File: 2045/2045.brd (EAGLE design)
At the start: 57.8 x 216.2 mm, 47 parts, among them IC1 OPA2134P, IC2 OPA2134P, X1 2516-

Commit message: upated the 2045 filter
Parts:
- added C13, C14: (no value), dan:E2,5-7
- added D4, D5, D6, D7: 1N4148DO35-7, dan:DO35-7
- added IN1POT, IN2POT: US-EVUF2J, dan:EVUFXJ
- added R25, R51: 10, dan:0207/2V
- C5, C6, C7: device dan:E3,5-10 -> dan:E2,5-7
- R1, R10, R11, R12, R13, R14, R15, R2, R3, R4, R5, R6, R7, R8, R9: device dan:0309/12 -> dan:0204/7
- moved C12 75.7 mm to (48.3, 15.2), turned to 270 degrees
- moved C11 55.5 mm to (22.2, 31.1), turned to 180 degrees
- moved IN2 23.8 mm to (44.5, 139.7)
- moved IN 23.7 mm to (14.0, 139.7)
- moved Q 23.3 mm to (45.1, 204.5)
- moved CVA 23.1 mm to (29.2, 184.8)
- moved R8 20.4 mm to (17.1, 154.3), turned to 0 degrees
- moved R15 18.8 mm to (43.8, 193.7), turned to 0 degrees
- moved CVIN 14.1 mm to (29.2, 139.7)
- moved 2POUT 10.3 mm to (44.5, 122.6)
- moved 4POUTPUT 10.0 mm to (14.0, 122.6)
- moved R7 9.94 mm to (41.3, 154.3), turned to 180 degrees
- moved R14 9.44 mm to (14.6, 191.8), turned to 180 degrees
- moved C6 7.62 mm to (49.5, 66.7)
- moved FC 7.41 mm to (13.3, 204.5)
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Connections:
- new net N$35: IN.P$3, IN1POT.3
- new net N$36: IN2.P$3, IN2POT.3
- new net N$37: D6.C, D7.C, R51.2
- new net N$38: D4.A, D5.A, R25.2
- new net N$71: D7.A, X1.10, X1.9
- new net N$72: D4.C, X1.1, X1.2
- net +12V: now also C13.+, R51.1; no longer X1.10, X1.9
- net -12V: now also C14.-, R25.1; no longer X1.1, X1.2
- net GND: now also C13.-, C14.+, D5.C, D6.A, IN1POT.1, IN2POT.1
- net N$15: now also IN1POT.2; no longer IN.P$3
- net N$29: now also IN2POT.2; no longer IN2.P$3
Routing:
- net N$15: track 53.6 -> 5.06 mm, vias 2 -> 0
- net N$27: track 58.6 -> 101.2 mm, vias 1 -> 0
- net N$29: track 47.5 -> 6.96 mm, vias 1 -> 0
- net -12V: track 329.8 -> 305.4 mm, vias 10 -> 7
- net N$23: track 92.5 -> 116.2 mm
- net N$5: track 47.3 -> 26.4 mm, vias 2 -> 1
- net N$7: track 7.66 -> 25.7 mm
- net N$36: track 0.00 -> 17.0 mm, vias 0 -> 1
- net N$31: track 69.1 -> 52.5 mm, vias 2 -> 0
- net +12V: track 274.5 -> 258.6 mm, vias 8 -> 7
- net N$35: track 0.00 -> 15.4 mm
- net N$72: track 0.00 -> 14.4 mm
- net N$32: track 59.5 -> 46.1 mm, vias 4 -> 0
- net N$71: track 0.00 -> 13.2 mm
- net N$26: track 79.0 -> 90.1 mm
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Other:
- board text added: "mutator"
- board text added: "ssm2045"
- board text removed: "SSM2045 filter"

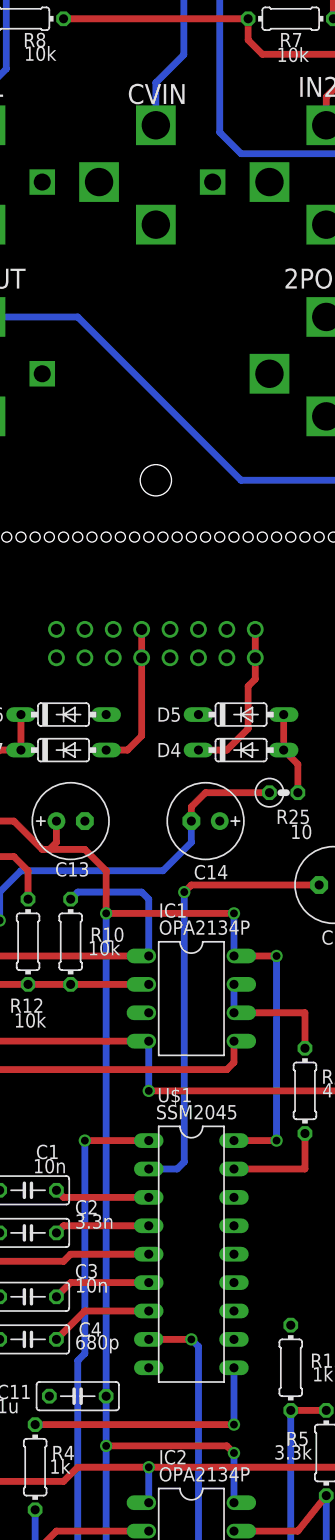
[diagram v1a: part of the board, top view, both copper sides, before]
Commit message: updated svf with dc offset trim pots and transistors for biasing
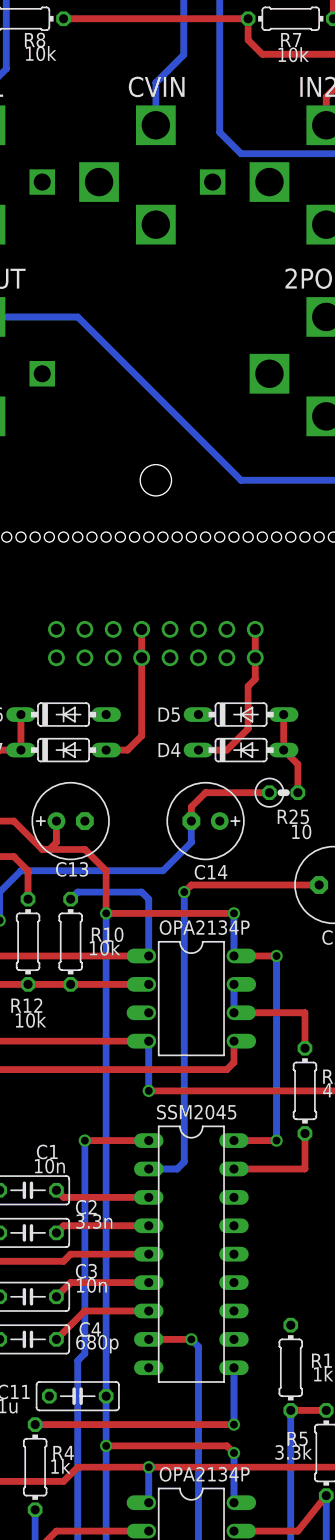
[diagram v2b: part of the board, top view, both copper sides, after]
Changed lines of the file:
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@@
 <text x="10.16" y="130.175" size="1.778" layer="21" font="vector" ratio="15">4POUT</text>
 <text x="40.64" y="130.175" size="1.778" layer="21" font="vector" ratio="15">2POUT</text>
-<text x="26.67" y="146.685" size="1.778" layer="21" font="vector" ratio="15">CVIN</text>
+<text x="26.67" y="147.32" size="1.778" layer="21" font="vector" ratio="15">CVIN</text>
 <text x="12.065" y="147.32" size="1.778" layer="21" font="vector" ratio="15">IN1</text>
 <text x="41.91" y="147.32" size="1.778" layer="21" font="vector" ratio="15">IN2</text>
@@
 </element>
 <element name="IC1" library="dan" package="DIL08" value="OPA2134P" x="32.385" y="66.675" smashed="yes" rot="R270">
-<attribute name="NAME" x="29.464" y="73.914" size="1.27" layer="21" font="vector" ratio="15"/>
 <attribute name="VALUE" x="29.464" y="72.39" size="1.27" layer="21" font="vector" ratio="15"/>
 </element>
 <element name="IC2" library="dan" package="DIL08" value="OPA2134P" x="32.385" y="17.78" smashed="yes" rot="R270">
-<attribute name="NAME" x="29.464" y="25.019" size="1.27" layer="21" font="vector" ratio="15"/>
 <attribute name="VALUE" x="29.464" y="23.495" size="1.27" layer="21" font="vector" ratio="15"/>
 </element>
@@
 </element>
 <element name="U$1" library="dan" package="DIL18" value="SSM2045" x="32.385" y="43.815" smashed="yes" rot="R270">
-<attribute name="NAME" x="29.337" y="57.404" size="1.27" layer="21" font="vector" ratio="15"/>
 <attribute name="VALUE" x="29.21" y="55.88" size="1.27" layer="21" font="vector" ratio="15"/>
 </element>
